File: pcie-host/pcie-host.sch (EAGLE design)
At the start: 243 parts, among them Q1 NDS351AN, Q2 NDS351AN, Q3 BSH103, Q4 BSH103, Q5 NDS351AN, U1 ISO, U10 LTM4622_BGA, U11 ISO1541DR, U12 S24SE12002, U13 ISO7240M, U14 ISO7240M, U15 ISO7240M, U16 ISO7240M, U17 ISO7242M, U18 COMM, U19 SN65LVDT388A, U20 SN65LVDS387, U21 SN65LVDS391, U4 SN74LVT125, U5 ADCMP600, U6 ADCMP600, U8 MCP47FEBX2, U9 DS90UB914A-Q1, X1 PCI-MECH_STD-H_HALF-W

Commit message: PCIe host board update
- Fixed term indicator LED circuit so that it does not short DI lines to
3.3V
- Connectoed power indication LED to power
- Fixed the LVDS driver footprints
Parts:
- removed C62, C63, C64, C65, C67, C68, C69, C70, C72, C73, C74, C75, C76, C77, C78, C79: (no value), jonnew:C_0402
- added R73, R74: 1k, jonnew:R_0603
- added R75: 1k, cyclops:R_0603
- R1, R2, R46: value 220 -> 1k
- R10, R8: value 2.2k -> 100k
- R11: value 820 -> 1k
- R16, R17, R21, R22, R23, R24: value 150, 0.25W -> 150,0.25W
- R9: value 820 -> 1k; device RHD2000_eval_board:R_0603 -> jonnew:R_0603
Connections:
- new net N$33: PWR/LOCK1.A, R75.1
- new net N$34: Q4.G, R74.2, R8.2
- new net N$37: Q3.G, R10.2, R73.2
- net +3V3: no longer R11.1, R9.1
- net +3V3_ISO: now also R75.2
- net +3V3_ISO_PG: no longer C79.1
- net D0: no longer C76.1
- net D1: no longer C72.1
- net D10: no longer C69.1
- net D11: no longer C64.1
- net D2: no longer C67.1
- net D3: no longer C62.1
- net D4: no longer C77.1
- net D5: no longer C73.1
- net D6: no longer C68.1
- net D7: no longer C63.1
- net D8: no longer C78.1
- net D9: no longer C74.1
- net DI0_TERM: now also R73.1, R9.1; no longer Q3.G, R10.2
- net DI1_TERM: now also R11.1, R74.1; no longer Q4.G, R8.2
- net GND: now also TERM1.C, TERM2.C; no longer C62.2, C63.2, C64.2, C65.2, C67.2, C68.2, C69.2, C70.2, C72.2, C73.2, C74.2, C75.2, C76.2, C77.2, C78.2, C79.2
- net GND_ISO: now also PWR/LOCK1.C
- net HSYNC: no longer C65.1
- net N$2: no longer TERM2.C
- net N$7: no longer TERM1.C
- net PCLK: no longer C75.1
- net VSYNC: no longer C70.1
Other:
- moved on the sheet: R10, R11, R8, R9, TERM1, TERM2, U1, U18

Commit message: PCIe host board revision 1.1
- Ready for fab
- Fixed I2C part number: ISO1540 instead of ISO1541
- More and larger testpoints
- Improved silkscreen
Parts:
- added TP23: GND, jonnew:TP_1MM
- added TP24: SDA, jonnew:TP_1MM
- added TP25: SCL, jonnew:TP_1MM
- added TP26: SCL(ISO), jonnew:TP_1MM
- added TP27: SDA(ISO), jonnew:TP_1MM
- added TP28: GND(ISO), jonnew:TP_1MM
- TP1, TP18, TP19, TP2, TP20: device jonnew:TP_0.035IN -> jonnew:TP_1MM
- TP10, TP11, TP12, TP13, TP14, TP15, TP16, TP17, TP21, TP22, TP3: device jonnew:TP_0.035IN -> jonnew:TP_2MM
- TP4: value +12V(ISO) -> +5.5V(ISO); device jonnew:TP_0.035IN -> jonnew:TP_2MM
- U11: value ISO1541DR -> ISO1540DR
- U12: value S24SE12002 -> UEI15-050-Q12P-C
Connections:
- net +12V_ISO renamed +5.5V_ISO
- net GND: now also TP23.TP
- net GND_ISO: now also TP28.TP
- net SCL: now also TP25.TP
- net SCL_ISO: now also TP26.TP
- net SDA: now also TP24.TP
- net SDA_ISO: now also TP27.TP
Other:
- note added: "UEI15 Choices: 12V: S24SE12002 w/ Rtrim = Inf 5.5V: UEI15-050-Q12P-C w/ Rtrm = 9.53k resistor"
- note removed: "DNP"
- note removed: "UEI15 Choices: 12V:S24SE12002 5.5V:UEI15-050-Q12P-C w/ 9.53k resistor"

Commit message: Added strain relief plates to PCIe host board
- There are 2 of them tabbed onto the PCIe deserializer board
- Press in nuts go on strain relief board and 4-40 screw go throut the
PCIe deserializer board to pull them onto the FMC connector.
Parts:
- X1: value PCI-MECH_STD-H_HALF-W -> PCI-MECH_STD-H_HALF-W_FMC-STRAIN; device jonnew:PCI-MECH_STD-H_HALF-W -> jonnew:PCI-MECH_STD-H_HALF-W_FMC-STRAIN
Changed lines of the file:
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@@
 <part name="TP3" library="jonnew" deviceset="TP" device="_2MM" value="+3.3V(ISO)"/>
 <part name="TP4" library="jonnew" deviceset="TP" device="_2MM" value="+5.5V(ISO)"/>
-<part name="X1" library="jonnew" deviceset="PCI-MECH" device="_STD-H_HALF-W"/>
+<part name="X1" library="jonnew" deviceset="PCI-MECH" device="_STD-H_HALF-W_FMC-STRAIN" value="PCI-MECH_STD-H_HALF-W_FMC-STRAIN"/>
 <part name="F3" library="jonnew" deviceset="FUSE" device="_1812" value="C014F-2"/>
 <part name="F1" library="jonnew" deviceset="FUSE" device="_1812" value="C014F-2"/>

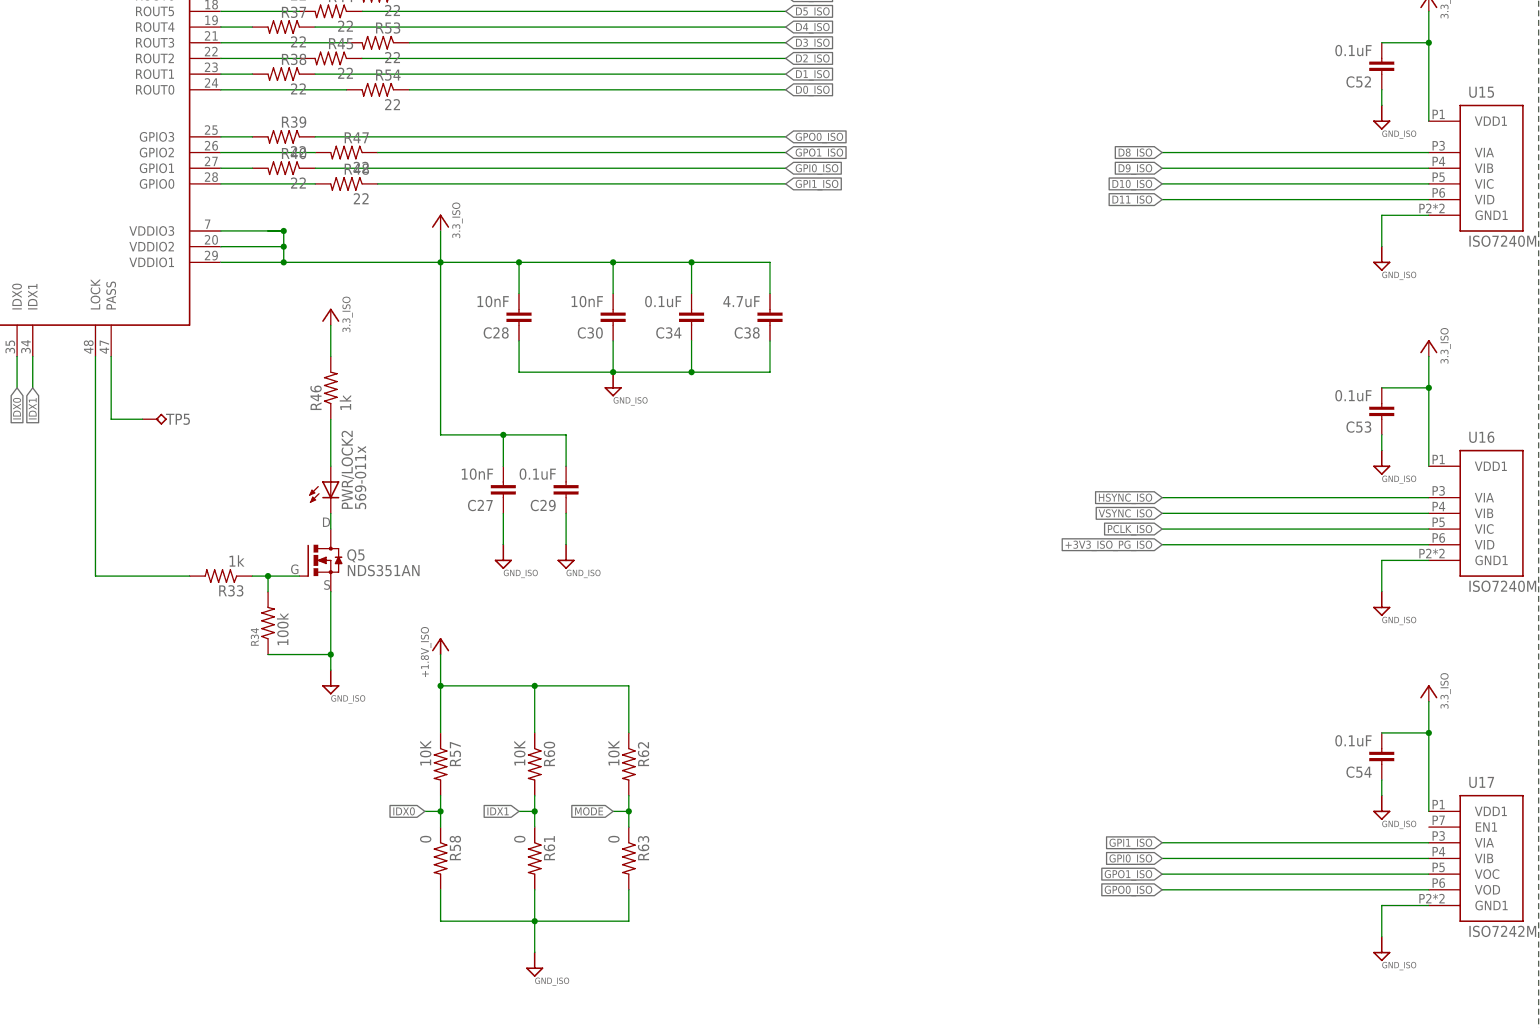
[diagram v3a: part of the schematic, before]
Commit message: Replaced GPIO3 with PASS on pcie-host board
- PASS pin from deserializer which goes low if errors are detected in
the deserialed payload. This can be use to detect bad frames even when
the lock to the serializer is maintained.
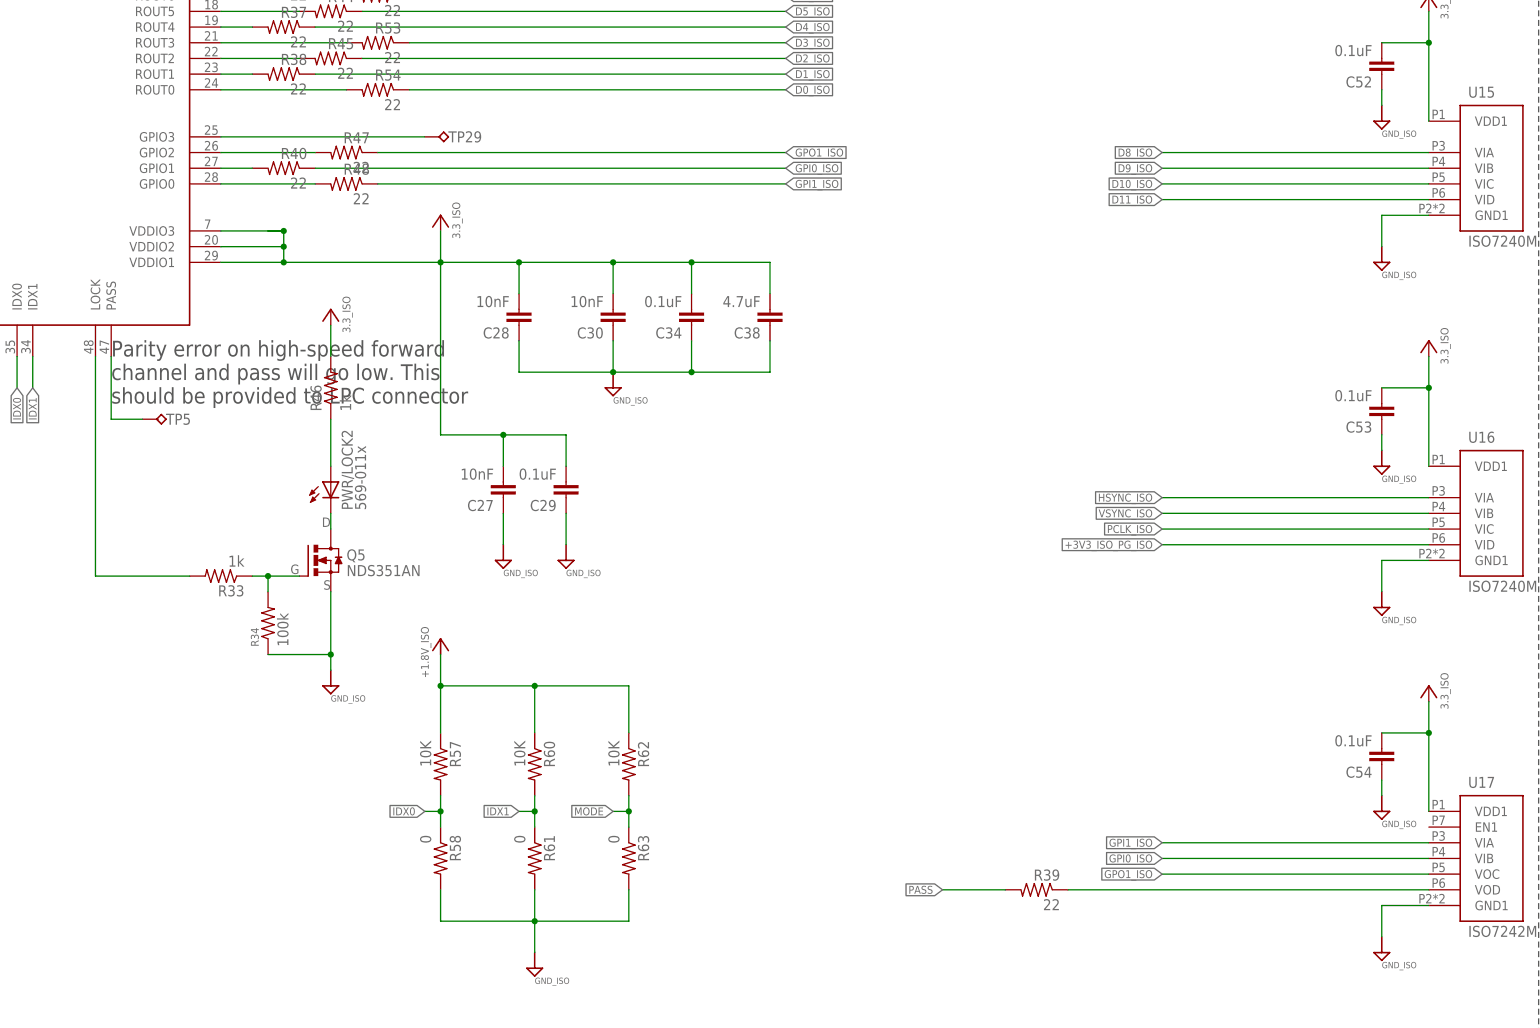
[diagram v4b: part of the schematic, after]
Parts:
- added TP29: GPIO3, jonnew:TPTP06R
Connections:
- net GPO0_ISO renamed N$1
- removed net N$1 (its old number): TP5.TP, U9.PASS
- removed net N$56: R39.2, U9.GPIO3
- new net N$38: TP29.TP, U9.GPIO3
- new net PASS: R39.2, TP5.TP, U9.PASS
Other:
- note added: "Parity error on high-speed forward channel and pass will go low. This should be provided to LPC connector"
- moved on the sheet: R39
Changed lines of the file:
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@@
 <part name="GND99" library="jonnew" deviceset="GND_ISO" device=""/>
 <part name="GND100" library="supply1" deviceset="GND" device=""/>
-<part name="R39" library="jonnew" deviceset="R" device="_0402" value="22"/>
 <part name="R47" library="jonnew" deviceset="R" device="_0402" value="22"/>
 <part name="R40" library="jonnew" deviceset="R" device="_0402" value="22"/>
@@
 <part name="TP27" library="jonnew" deviceset="TP" device="_1MM" value="SDA(ISO)"/>
 <part name="TP28" library="jonnew" deviceset="TP" device="_1MM" value="GND(ISO)"/>
+<part name="R39" library="jonnew" deviceset="R" device="_0402" value="22"/>
+<part name="TP29" library="jonnew" deviceset="TP" device="TP06R" value="GPIO3"/>
 </parts>
 <sheets>
@@
 <text x="624.84" y="322.58" size="2.54" layer="97">SN65LVDT388A has integrated
 110 ohm term resistors.</text>
+<text x="236.22" y="106.68" size="2.54" layer="97">Parity error on high-speed forward
+channel and pass will go low. This
+should be provided to LPC connector</text>
 </plain>
 <instances>
@@
 <instance part="GND99" gate="G$1" x="441.96" y="43.18"/>
 <instance part="GND100" gate="1" x="487.68" y="15.24"/>
-<instance part="R39" gate="R" x="264.16" y="149.86" rot="MR0"/>
 <instance part="R47" gate="R" x="274.32" y="147.32" rot="MR0"/>
 <instance part="R40" gate="R" x="264.16" y="144.78" rot="MR0"/>
@@
 <instance part="TP27" gate="G$1" x="408.94" y="388.62" rot="R180"/>
 <instance part="TP28" gate="G$1" x="416.56" y="388.62" rot="R180"/>
+<instance part="R39" gate="R" x="386.08" y="27.94" rot="MR0"/>
+<instance part="TP29" gate="G$1" x="289.56" y="149.86" rot="R270"/>
 </instances>
 <busses>
@@
 </segment>
 </net>
-<net name="N$56" class="0">
-<segment>
-<wire x1="254" y1="149.86" x2="259.08" y2="149.86" width="0.1524" layer="91"/>
-<pinref part="R39" gate="R" pin="2"/>
-<pinref part="U9" gate="G$1" pin="GPIO3"/>
-</segment>
-</net>
 <net name="N$57" class="0">
 <segment>
@@
 </segment>
 </net>
-<net name="GPO0_ISO" class="0">
-<segment>
-<wire x1="449.58" y1="27.94" x2="406.4" y2="27.94" width="0.1524" layer="91"/>
-<pinref part="U17" gate="G$1" pin="VOD"/>
-<label x="406.4" y="27.94" size="1.27" layer="95" rot="R180" xref="yes"/>
-</segment>
-<segment>
-<pinref part="R39" gate="R" pin="1"/>
-<label x="345.44" y="149.86" size="1.27" layer="95" xref="yes"/>
-<wire x1="269.24" y1="149.86" x2="345.44" y2="149.86" width="0.1524" layer="91"/>
-</segment>
-</net>
-<net name="N$1" class="0">
-<segment>
-<wire x1="241.3" y1="104.14" x2="236.22" y2="104.14" width="0.1524" layer="91"/>
-<wire x1="236.22" y1="104.14" x2="236.22" y2="114.3" width="0.1524" layer="91"/>
-<pinref part="TP5" gate="G$1" pin="TP"/>
-<pinref part="U9" gate="G$1" pin="PASS"/>
-</segment>
-</net>
 <net name="PCLK_N" class="1">
 <segment>
@@
 <net name="GPO1_ISO" class="0">
 <segment>
-<pinref part="U17" gate="G$1" pin="VOC"/>
-<wire x1="449.58" y1="30.48" x2="406.4" y2="30.48" width="0.1524" layer="91"/>
-<label x="406.4" y="30.48" size="1.27" layer="95" rot="R180" xref="yes"/>
-</segment>
-<segment>
 <label x="345.44" y="147.32" size="1.27" layer="95" xref="yes"/>
 <pinref part="R47" gate="R" pin="1"/>
 <wire x1="345.44" y1="147.32" x2="279.4" y2="147.32" width="0.1524" layer="91"/>
 </segment>
+<segment>
+<label x="406.4" y="30.48" size="1.27" layer="95" rot="R180" xref="yes"/>
+<pinref part="U17" gate="G$1" pin="VOC"/>
+<wire x1="449.58" y1="30.48" x2="406.4" y2="30.48" width="0.1524" layer="91"/>
+</segment>
 </net>
 <net name="+5.5V_ISO" class="0">
@@
 </segment>
 </net>
+<net name="PASS" class="0">
+<segment>
+<wire x1="241.3" y1="104.14" x2="236.22" y2="104.14" width="0.1524" layer="91"/>
+<wire x1="236.22" y1="104.14" x2="236.22" y2="114.3" width="0.1524" layer="91"/>
+<pinref part="TP5" gate="G$1" pin="TP"/>
+<pinref part="U9" gate="G$1" pin="PASS"/>
+</segment>
+<segment>
+<wire x1="381" y1="27.94" x2="370.84" y2="27.94" width="0.1524" layer="91"/>
+<label x="370.84" y="27.94" size="1.27" layer="95" rot="R180" xref="yes"/>
+<pinref part="R39" gate="R" pin="2"/>
+</segment>
+</net>
+<net name="N$38" class="0">
+<segment>
+<pinref part="U9" gate="G$1" pin="GPIO3"/>
+<pinref part="TP29" gate="G$1" pin="TP"/>
+<wire x1="254" y1="149.86" x2="287.02" y2="149.86" width="0.1524" layer="91"/>
+</segment>
+</net>
+<net name="N$1" class="0">
+<segment>
+<pinref part="R39" gate="R" pin="1"/>
+<pinref part="U17" gate="G$1" pin="VOD"/>
+<wire x1="391.16" y1="27.94" x2="449.58" y2="27.94" width="0.1524" layer="91"/>
+</segment>
+</net>

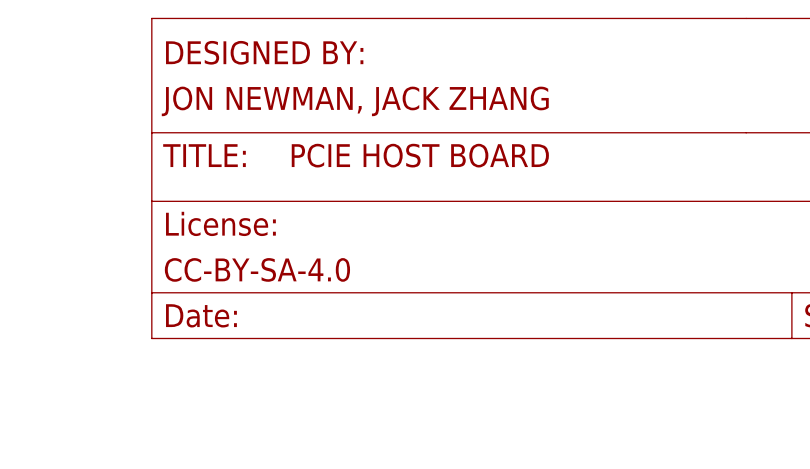
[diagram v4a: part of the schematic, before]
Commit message: Lots of small fixes and cleanup
- Taking care of little issues that have been bothering me
- Dediated serdes interface board moved to deprecated
- Non-serialized headstage moved to deprecated
- Deleted top-level datasheets directory which does not really
apply to anything anymore
- Added pdfs versions of board schematics so that eagle is not
needed to see them.
- Small fixes to test-boards: High power LEDs moved to bottom to prevent
blinding ppl. Silkscreen improved. License updated. Etc. Gerbers
updated.
- Removed random deprecated design files where I found them.
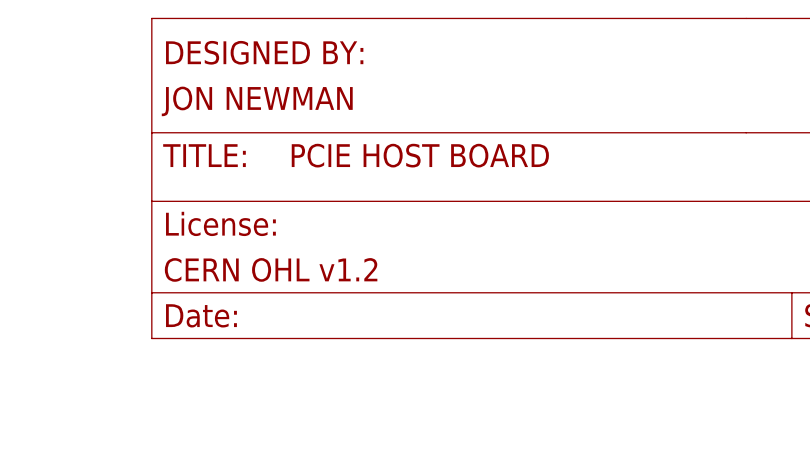
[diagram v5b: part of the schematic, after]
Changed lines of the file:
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@@
 <schematic xreflabel="%F%N/%S.%C%R" xrefpart="/%S.%C%R">
 <attributes>
-<attribute name="DESIGNER" value="JON NEWMAN, JACK ZHANG"/>
+<attribute name="DESIGNER" value="JON NEWMAN"/>
 <attribute name="DESIGN_NAME" value="PCIE HOST BOARD"/>
-<attribute name="LICENSE" value="CC-BY-SA-4.0"/>
+<attribute name="LICENSE" value="CERN OHL v1.2"/>
 <attribute name="REVISION" value="1.1"/>
 </attributes>
